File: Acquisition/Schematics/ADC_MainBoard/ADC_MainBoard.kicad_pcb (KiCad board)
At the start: 2 copper layers, 44.4 x 33 mm, 49 parts, among them J1 Conn_02x06_Counter_Clockwise, J13 Conn_01x02_Pin, J14 Pad, J15 Pad, J16 Pad, J17 Pad, J2 Pad, J3 Pad, J5 2004850720, J6 Conn_02x06_Counter_Clockwise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

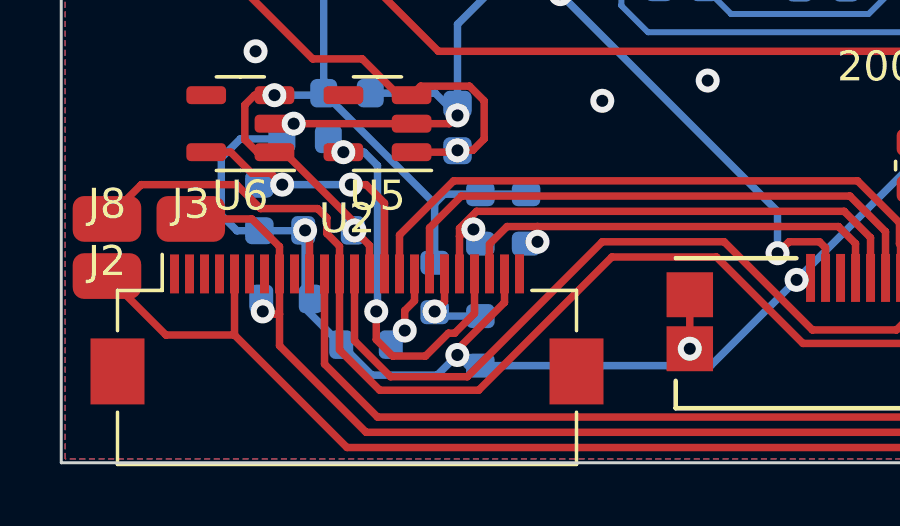
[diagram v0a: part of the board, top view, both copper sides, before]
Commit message: ADC board prototype - ORDER
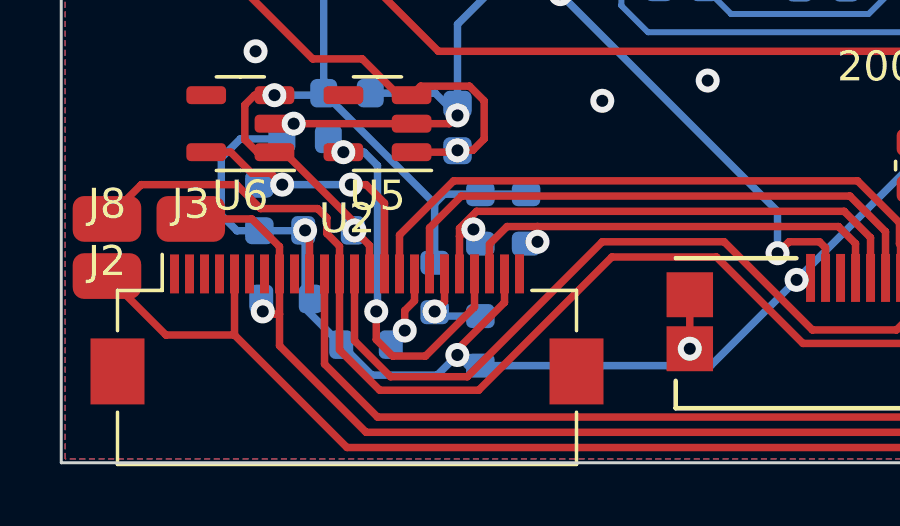
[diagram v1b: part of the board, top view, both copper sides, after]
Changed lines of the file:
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@@
     (pad_to_mask_clearance 0)
     (pcbplotparams
-      (layerselection 0x00010fc_ffffffff)
+      (layerselection 0x00010c0_ffffffff)
       (plot_on_all_layers_selection 0x0000000_00000000)
       (disableapertmacros false)
@@
       (outputformat 1)
       (mirror false)
-      (drillshape 1)
+      (drillshape 0)
       (scaleselection 1)
       (outputdirectory "")
@@
   (segment (start 66.575 64.58) (end 66.421 64.426) (width 0.25) (layer "B.Cu") (net 9))
   (segment (start 67.945 64.58) (end 66.575 64.58) (width 0.25) (layer "B.Cu") (net 9))
-  (segment (start 66.116042 65.913) (end 66.878042 65.151) (width 0.25) (layer "F.Cu") (net 10))
-  (segment (start 67.75 64.487604) (end 67.75 63.174) (width 0.25) (layer "F.Cu") (net 10))
   (segment (start 64.475 65.364) (end 65.024 65.913) (width 0.25) (layer "F.Cu") (net 10))
-  (segment (start 66.878042 65.151) (end 67.086604 65.151) (width 0.25) (layer "F.Cu") (net 10))
-  (segment (start 67.086604 65.151) (end 67.75 64.487604) (width 0.25) (layer "F.Cu") (net 10))
+  (segment (start 67.75 64.279042) (end 67.75 63.174) (width 0.25) (layer "F.Cu") (net 10))
+  (segment (start 65.024 65.913) (end 66.116042 65.913) (width 0.25) (layer "F.Cu") (net 10))
   (segment (start 64.475 64.424002) (end 64.475 65.364) (width 0.25) (layer "F.Cu") (net 10))
-  (segment (start 65.024 65.913) (end 66.116042 65.913) (width 0.25) (layer "F.Cu") (net 10))
+  (segment (start 66.116042 65.913) (end 67.75 64.279042) (width 0.25) (layer "F.Cu") (net 10))
   (via (at 63.3785 59.116) (size 0.8) (drill 0.4) (layers "F.Cu" "B.Cu") (net 10))
   (via (at 64.475 64.424002) (size 0.8) (drill 0.4) (layers "F.Cu" "B.Cu") (net 10))
